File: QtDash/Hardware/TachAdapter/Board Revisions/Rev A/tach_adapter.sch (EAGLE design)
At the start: 11 parts, among them IC1 PS2701-1

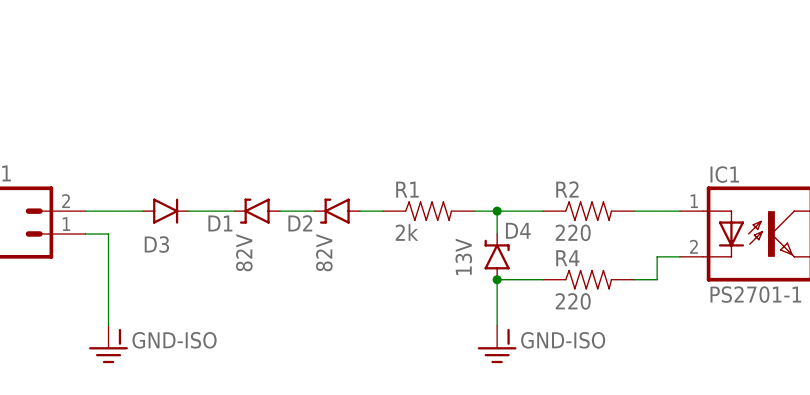
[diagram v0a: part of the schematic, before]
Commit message: - added assembly variant of Rev A tach adapter board -- with notes on final assembly 	- updated pdf of Rev A schematic with Rev A final assembly variant
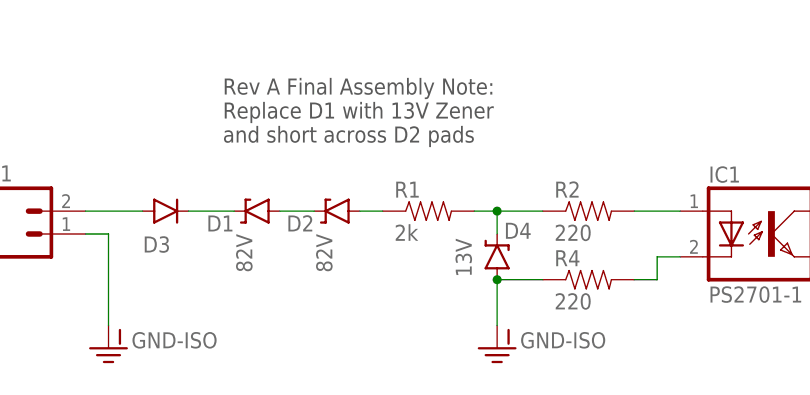
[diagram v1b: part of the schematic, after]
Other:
- note added: "Rev A Final Assembly Note: Replace D1 with 13V Zener and short across D2 pads"
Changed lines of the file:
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@@
 </attributes>
 <variantdefs>
+<variantdef name="Rev A Final" current="yes"/>
 </variantdefs>
 <classes>
@@
 <parts>
 <part name="D1" library="SparkFun-DiscreteSemi" deviceset="DIODE-ZENER" device="SMB" value="82V"/>
-<part name="D2" library="SparkFun-DiscreteSemi" deviceset="DIODE-ZENER" device="SMB" value="82V"/>
+<part name="D2" library="SparkFun-DiscreteSemi" deviceset="DIODE-ZENER" device="SMB" value="82V">
+<variant name="Rev A Final" populate="no"/>
+</part>
 <part name="D3" library="SparkFun-DiscreteSemi" deviceset="DIODE" device="SMA"/>
 <part name="R1" library="SparkFun-Passives" deviceset="RESISTOR" device="1206" value="2k"/>
@@
 <part name="SUPPLY1" library="SparkFun-Aesthetics" deviceset="3.3V" device=""/>
 <part name="GND1" library="SparkFun-Aesthetics" deviceset="GND" device=""/>
-<part name="D4" library="SparkFun-DiscreteSemi" deviceset="DIODE-ZENER" device="SMB" value="13V"/>
+<part name="D4" library="SparkFun-DiscreteSemi" deviceset="DIODE-ZENER" device="SMB" value="13V">
+<variant name="Rev A Final" populate="no"/>
+</part>
 <part name="GND-ISO2" library="SparkFun-Aesthetics" deviceset="GND-ISO" device=""/>
 <part name="J1" library="SparkFun-Connectors" deviceset="M02" device="PTH3"/>
@@
 <sheet>
 <plain>
+<text x="40.64" y="68.58" size="1.778" layer="97">Rev A Final Assembly Note:
+Replace D1 with 13V Zener
+and short across D2 pads</text>
 </plain>
 <instances>
@@
 </schematic>
 </drawing>
+<compatibility>
+<note version="6.3" minversion="6.2.2" severity="warning">
+Since Version 6.2.2 text objects can contain more than one line,
+which will not be processed correctly with this version.
+</note>
+</compatibility>
 </eagle>

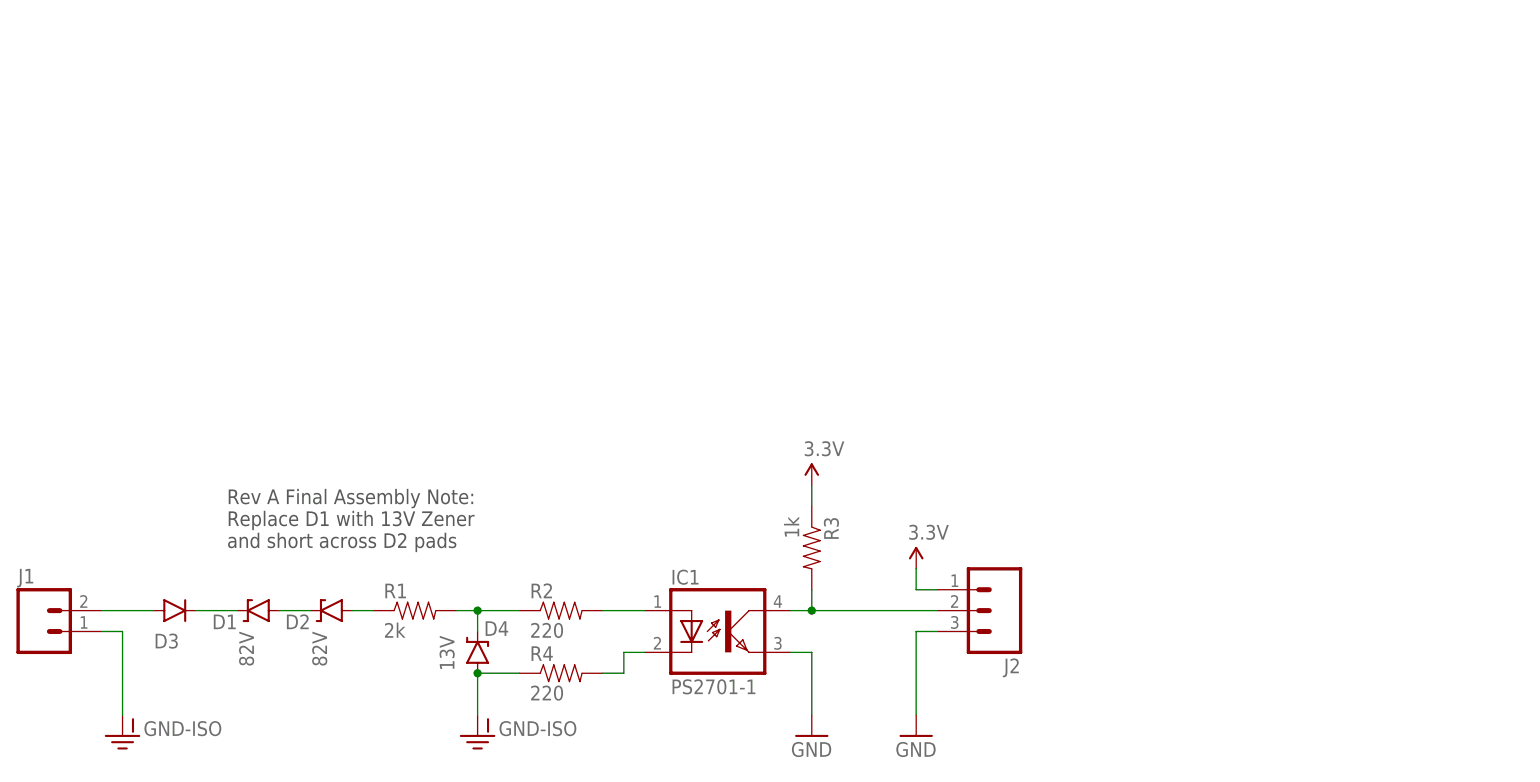
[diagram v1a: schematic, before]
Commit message: topic/documentation-update: 	- added tach adapter revision documentation for kicad and eagle
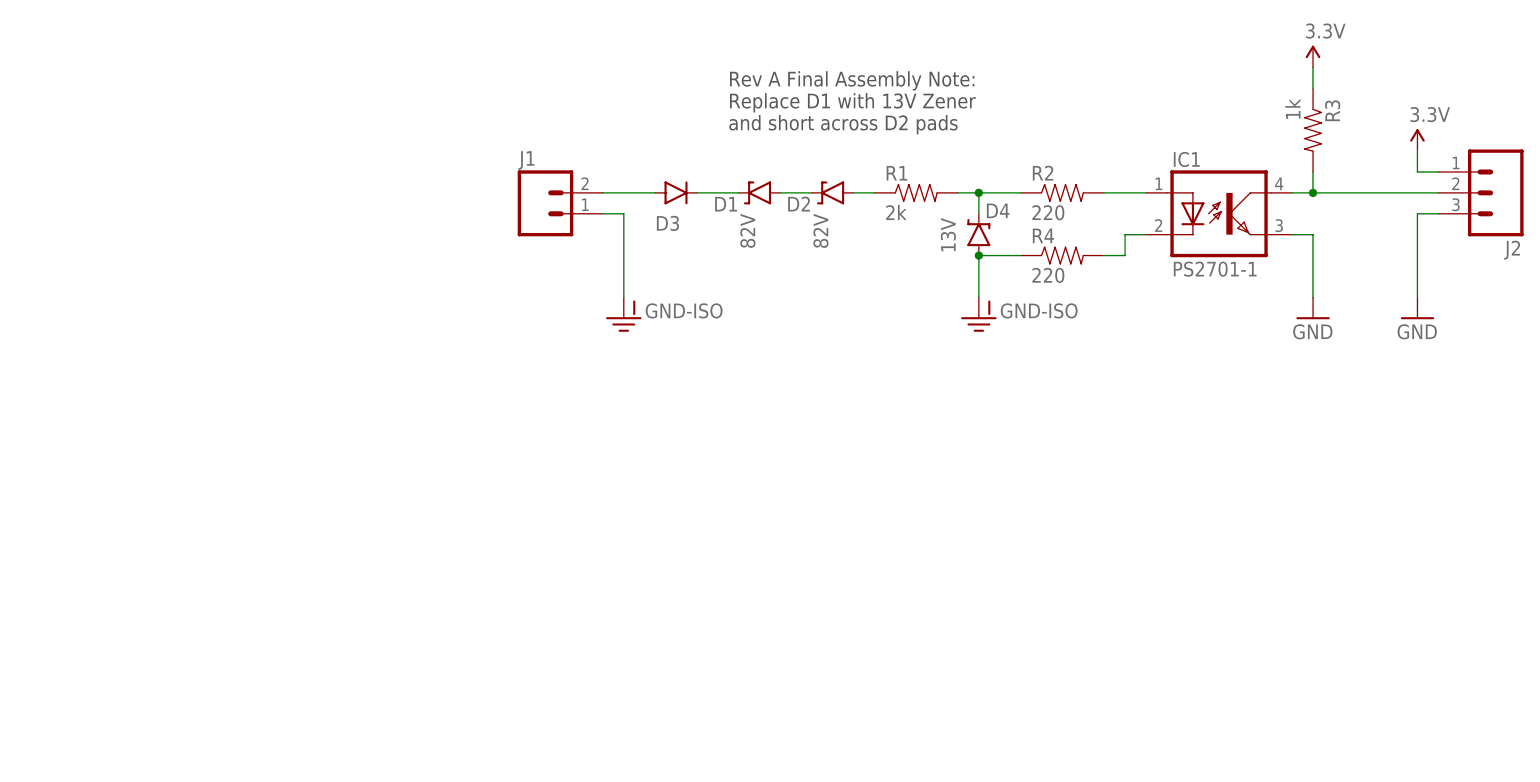
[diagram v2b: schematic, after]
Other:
- moved on the sheet: D1, D2, D3, D4, IC1, J1, J2, R1, R2, R3, R4
